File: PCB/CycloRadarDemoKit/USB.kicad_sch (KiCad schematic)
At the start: 41 parts, among them J301 USB_C_Receptacle_USB2.0, Q301 L8050QLT1G, Q302 L8050QLT1G, U301 CP2102N-Axx-xQFN28

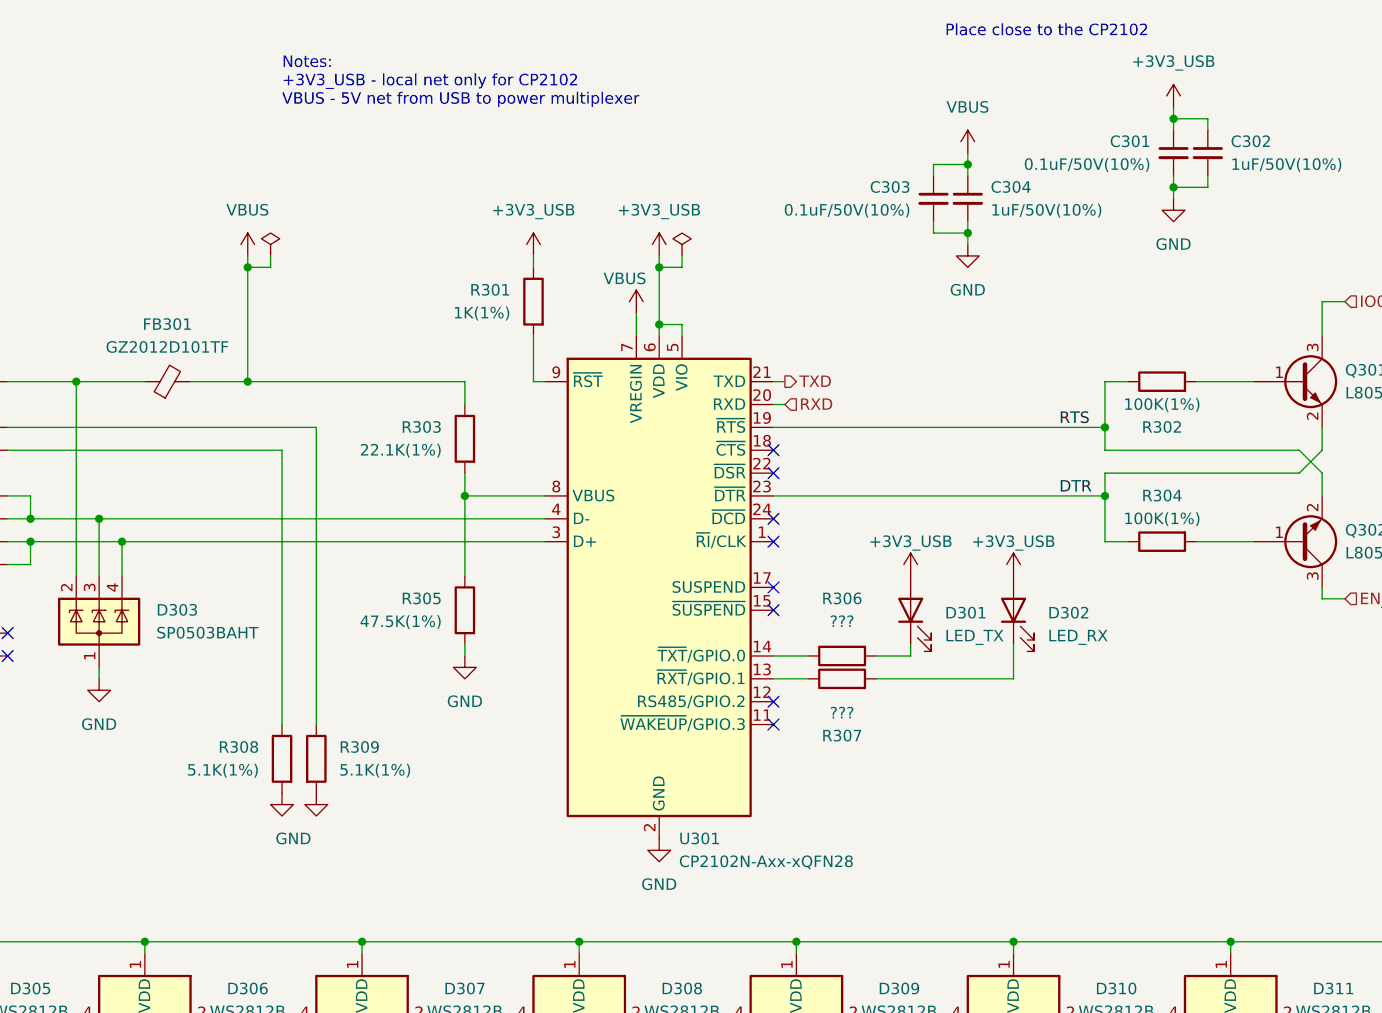
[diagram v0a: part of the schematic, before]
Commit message: added more LCSC parts
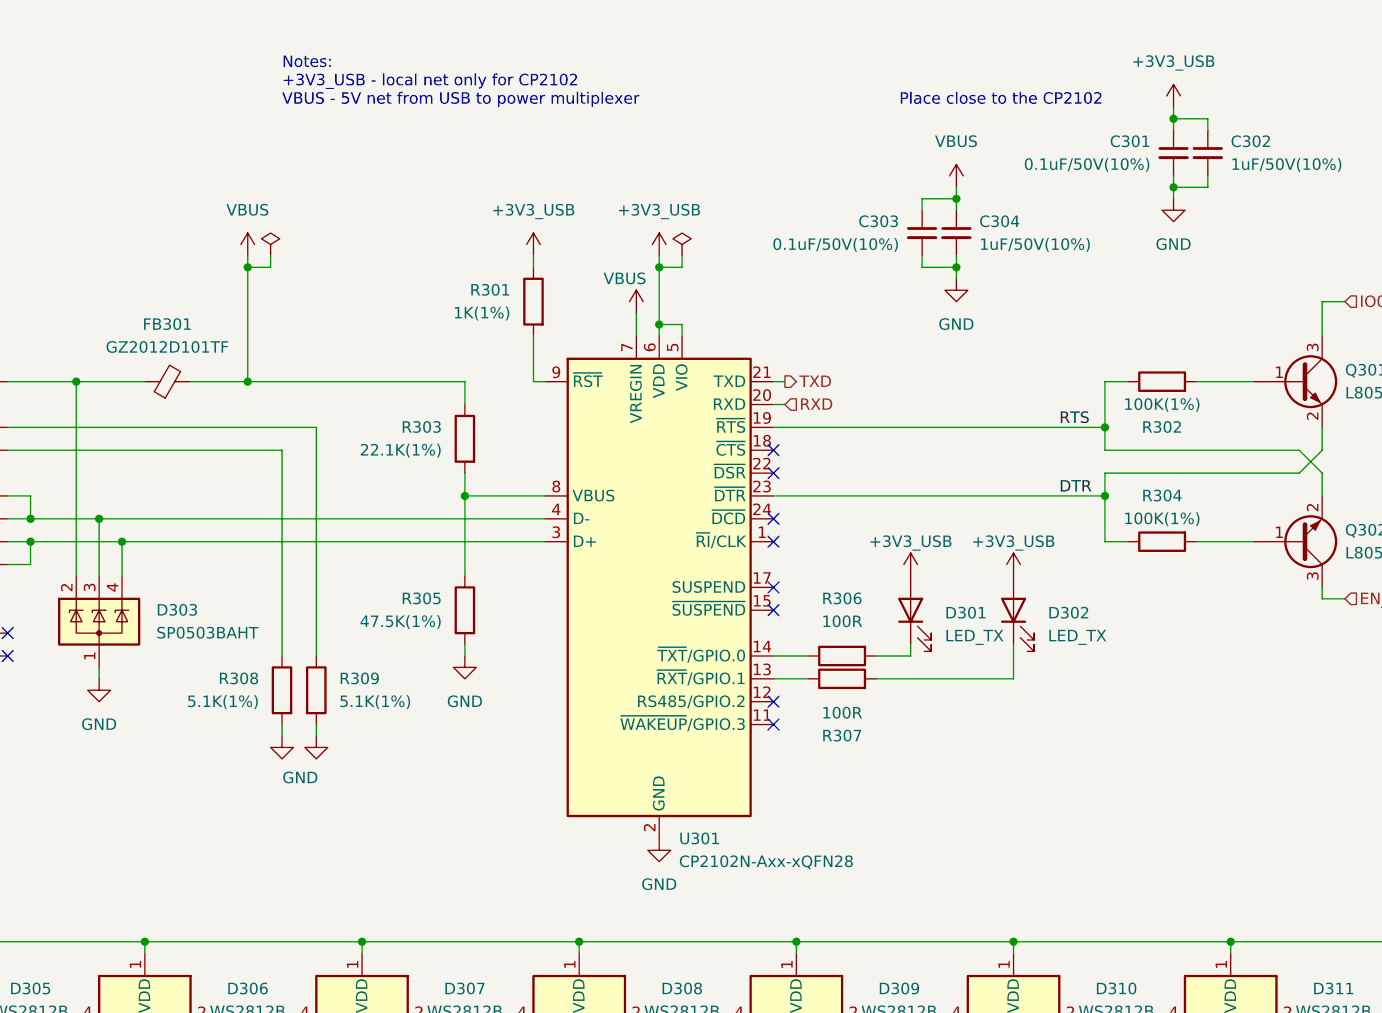
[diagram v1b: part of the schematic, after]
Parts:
- D301: footprint (none) -> LED_SMD:LED_0603_1608Metric; LCSC (none) -> C3028830
- D302: value LED_RX -> LED_TX; footprint (none) -> LED_SMD:LED_0603_1608Metric; LCSC (none) -> C3028830
- R301: footprint (none) -> Resistor_SMD:R_0603_1608Metric; LCSC (none) -> C21190
- R302, R304: footprint (none) -> Resistor_SMD:R_0603_1608Metric; LCSC (none) -> C25803
- R303: footprint (none) -> Resistor_SMD:R_0603_1608Metric; LCSC (none) -> C25961
- R305: footprint (none) -> Resistor_SMD:R_0603_1608Metric; LCSC (none) -> C23061
- R306, R307: value ??? -> 100R; footprint (none) -> Resistor_SMD:R_0603_1608Metric; LCSC (none) -> C22775
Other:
- moved on the sheet: C303, C304, R308, R309

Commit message: PCB ready for review
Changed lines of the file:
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@@
     (stroke (width 0) (type default))
   )
-  (wire (pts (xy 220.98 46.99) (xy 223.52 46.99))
+  (wire (pts (xy 220.98 49.53) (xy 223.52 49.53))
     (stroke (width 0) (type default))
   )
@@
     (stroke (width 0) (type default))
   )
-  (wire (pts (xy 220.98 50.8) (xy 220.98 46.99))
+  (wire (pts (xy 220.98 50.8) (xy 220.98 49.53))
     (stroke (width 0) (type default))
   )
@@
     (effects (font (size 1.27 1.27)) (justify left bottom))
   )
-  (hierarchical_label "IO0_AUTO" (shape input) (at 223.52 46.99 0) (fields_autoplaced)
+  (hierarchical_label "IO0_AUTO" (shape input) (at 223.52 49.53 0) (fields_autoplaced)
     (effects (font (size 1.27 1.27)) (justify left))
   )

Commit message: PCB after review
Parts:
- removed C301, C303: 0.1uF/50V(10%), Capacitor_SMD:C_0603_1608Metric, symbol Device:C_Small
- removed D304, D305, D306, D307, D308, D309, D310, D311, D312, D313, D314, D315, D316, D317, D318, D319, D320, D321, D322, D323: WS2812B, LED_SMD:LED_SK6812MINI_PLCC4_3.5x3.5mm_P1.75mm, symbol LED:WS2812B
- FB301: value GZ2012D101TF -> YI160808Z101-3R0T; footprint (none) -> Resistor_SMD:R_0603_1608Metric; LCSC (none) -> C3011210
- J301: footprint (none) -> Connector_USB:USB_C_Receptacle_GCT_USB4110; LCSC (none) -> C5260486
- renumbered C304 to C301
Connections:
- no-connect marks 12 -> 11
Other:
- note removed: "Place close to the CP2102"
- company: Alps Electric Czech, s.r.o. -> ALPS Electric Czech, s.r.o.
- title: Development module for Radar Safety Sensor -> Safety Ride Radar Sensor
- moved on the sheet: C301, C302, D301, D302, D303, FB301, J301, Q301, Q302, R301, R302, R303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

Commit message: updated readme
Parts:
- U301: value CP2102N-Axx-xQFN28 -> CP2102N-Axx-xQFN24
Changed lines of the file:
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@@
       (effects (font (size 1.27 1.27)) (justify left))
     )
-    (property "Value" "CP2102N-Axx-xQFN28" (at 159.6741 139.7 0)
+    (property "Value" "CP2102N-Axx-xQFN24" (at 159.6741 139.7 0)
       (effects (font (size 1.27 1.27)) (justify left))
     )

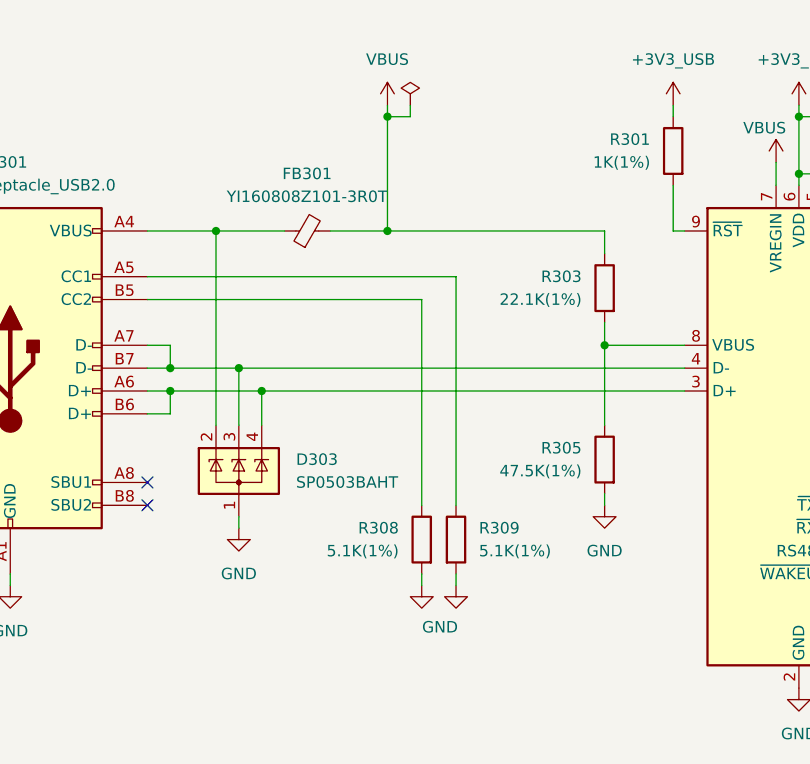
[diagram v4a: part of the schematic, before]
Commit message: schematic cosmetics, power management diagram upgrated
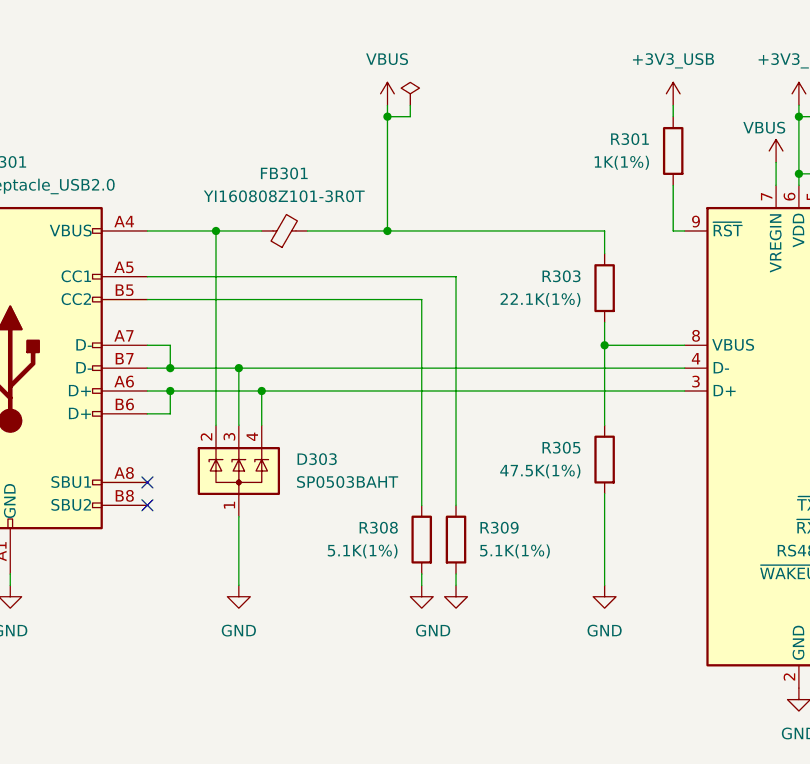
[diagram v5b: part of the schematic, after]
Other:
- moved on the sheet: FB301
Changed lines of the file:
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@@
     (stroke (width 0) (type default))
   )
-  (wire (pts (xy 95.25 118.11) (xy 95.25 119.38))
+  (wire (pts (xy 95.25 118.11) (xy 95.25 125.73))
     (stroke (width 0) (type default))
   )
@@
     (stroke (width 0) (type default))
   )
-  (wire (pts (xy 105.41 86.36) (xy 111.76 86.36))
+  (wire (pts (xy 102.87 86.36) (xy 111.76 86.36))
     (stroke (width 0) (type default))
   )
@@
     (stroke (width 0) (type default))
   )
-  (wire (pts (xy 92.71 86.36) (xy 100.33 86.36))
+  (wire (pts (xy 92.71 86.36) (xy 97.79 86.36))
     (stroke (width 0) (type default))
   )
@@
     (stroke (width 0) (type default))
   )
-  (wire (pts (xy 135.89 115.57) (xy 135.89 116.84))
+  (wire (pts (xy 135.89 115.57) (xy 135.89 125.73))
     (stroke (width 0) (type default))
   )
@@
     (effects (font (size 1.27 1.27)) (justify left))
   )
-  (symbol (lib_id "power:GND") (at 135.89 116.84 0) (unit 1)
-    (in_bom yes) (on_board yes) (dnp no) (fields_autoplaced)
-    (property "Reference" "#PWR0311" (at 135.89 123.19 0)
-      (effects (font (size 1.27 1.27)) hide)
-    )
-    (property "Value" "GND" (at 135.89 121.92 0)
-      (effects (font (size 1.27 1.27)))
-    )
-    (property "Footprint" "" (at 135.89 116.84 0)
-      (effects (font (size 1.27 1.27)) hide)
-    )
-    (property "Datasheet" "" (at 135.89 116.84 0)
+  (symbol (lib_id "power:GND") (at 135.89 125.73 0) (unit 1)
+    (in_bom yes) (on_board yes) (dnp no) (fields_autoplaced)
+    (property "Reference" "#PWR0311" (at 135.89 132.08 0)
+      (effects (font (size 1.27 1.27)) hide)
+    )
+    (property "Value" "GND" (at 135.89 130.81 0)
+      (effects (font (size 1.27 1.27)))
+    )
+    (property "Footprint" "" (at 135.89 125.73 0)
+      (effects (font (size 1.27 1.27)) hide)
+    )
+    (property "Datasheet" "" (at 135.89 125.73 0)
       (effects (font (size 1.27 1.27)) hide)
     )
@@
       (effects (font (size 1.27 1.27)) hide)
     )
-    (property "Value" "GND" (at 117.6006 130.3838 0)
+    (property "Value" "GND" (at 116.84 130.81 0)
       (effects (font (size 1.27 1.27)))
     )
@@
     )
   )
-  (symbol (lib_id "power:GND") (at 95.25 119.38 0) (unit 1)
-    (in_bom yes) (on_board yes) (dnp no) (fields_autoplaced)
-    (property "Reference" "#PWR0312" (at 95.25 125.73 0)
-      (effects (font (size 1.27 1.27)) hide)
-    )
-    (property "Value" "GND" (at 95.25 124.46 0)
-      (effects (font (size 1.27 1.27)))
-    )
-    (property "Footprint" "" (at 95.25 119.38 0)
-      (effects (font (size 1.27 1.27)) hide)
-    )
-    (property "Datasheet" "" (at 95.25 119.38 0)
+  (symbol (lib_id "power:GND") (at 95.25 125.73 0) (unit 1)
+    (in_bom yes) (on_board yes) (dnp no) (fields_autoplaced)
+    (property "Reference" "#PWR0312" (at 95.25 132.08 0)
+      (effects (font (size 1.27 1.27)) hide)
+    )
+    (property "Value" "GND" (at 95.25 130.81 0)
+      (effects (font (size 1.27 1.27)))
+    )
+    (property "Footprint" "" (at 95.25 125.73 0)
+      (effects (font (size 1.27 1.27)) hide)
+    )
+    (property "Datasheet" "" (at 95.25 125.73 0)
       (effects (font (size 1.27 1.27)) hide)
     )
@@
     )
   )
-  (symbol (lib_id "Device:FerriteBead_Small") (at 102.87 86.36 90) (unit 1)
-    (in_bom yes) (on_board yes) (dnp no) (fields_autoplaced)
-    (property "Reference" "FB301" (at 102.8319 80.01 90)
-      (effects (font (size 1.27 1.27)))
-    )
-    (property "Value" "YI160808Z101-3R0T" (at 102.8319 82.55 90)
-      (effects (font (size 1.27 1.27)))
-    )
-    (property "Footprint" "Resistor_SMD:R_0603_1608Metric" (at 102.87 88.138 90)
-      (effects (font (size 1.27 1.27)) hide)
-    )
-    (property "Datasheet" "~" (at 102.87 86.36 0)
-      (effects (font (size 1.27 1.27)) hide)
-    )
-    (property "LCSC" "C3011210" (at 102.87 86.36 0)
-      (effects (font (size 1.27 1.27)) hide)
-    )
+  (symbol (lib_id "Device:FerriteBead_Small") (at 100.33 86.36 90) (unit 1)
+    (in_bom yes) (on_board yes) (dnp no) (fields_autoplaced)
+    (property "Reference" "FB301" (at 100.2919 80.01 90)
+      (effects (font (size 1.27 1.27)))
+    )
+    (property "Value" "YI160808Z101-3R0T" (at 100.2919 82.55 90)
+      (effects (font (size 1.27 1.27)))
+    )
+    (property "Footprint" "Resistor_SMD:R_0603_1608Metric" (at 100.33 88.138 90)
+      (effects (font (size 1.27 1.27)) hide)
+    )
+    (property "Datasheet" "~" (at 100.33 86.36 0)
+      (effects (font (size 1.27 1.27)) hide)
+    )
+    (property "LCSC" "C3011210" (at 100.33 86.36 0)
+      (effects (font (size 1.27 1.27)) hide)
+    )

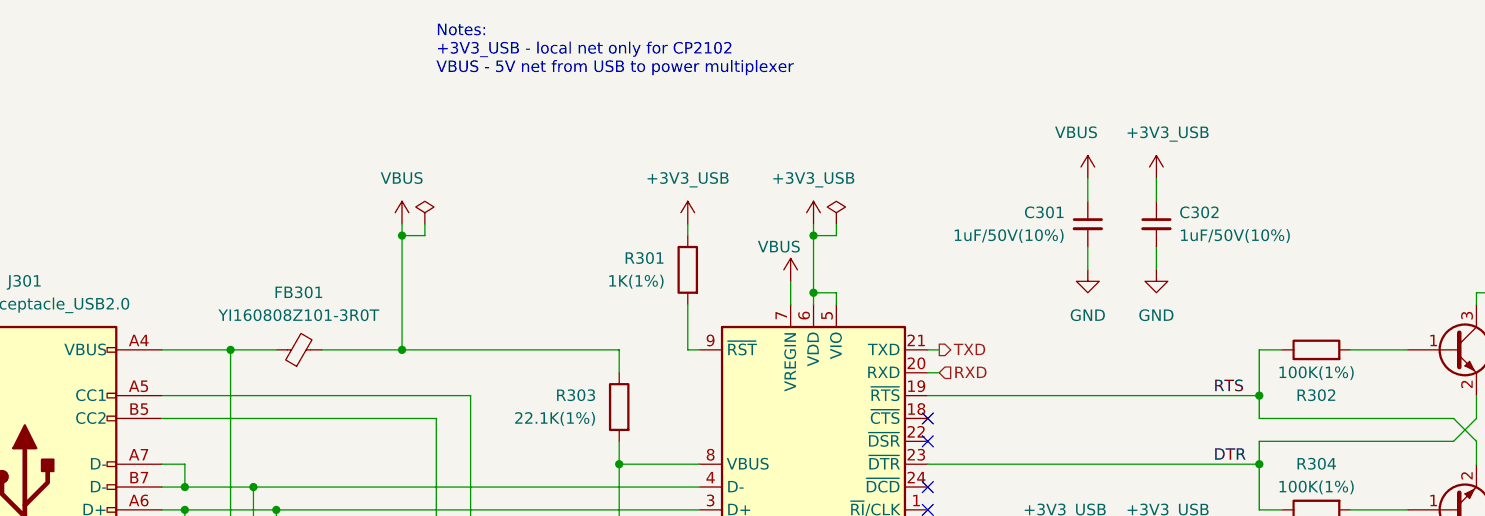
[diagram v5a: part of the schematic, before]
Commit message: Schematic edited, split sheets
improved PM diagram
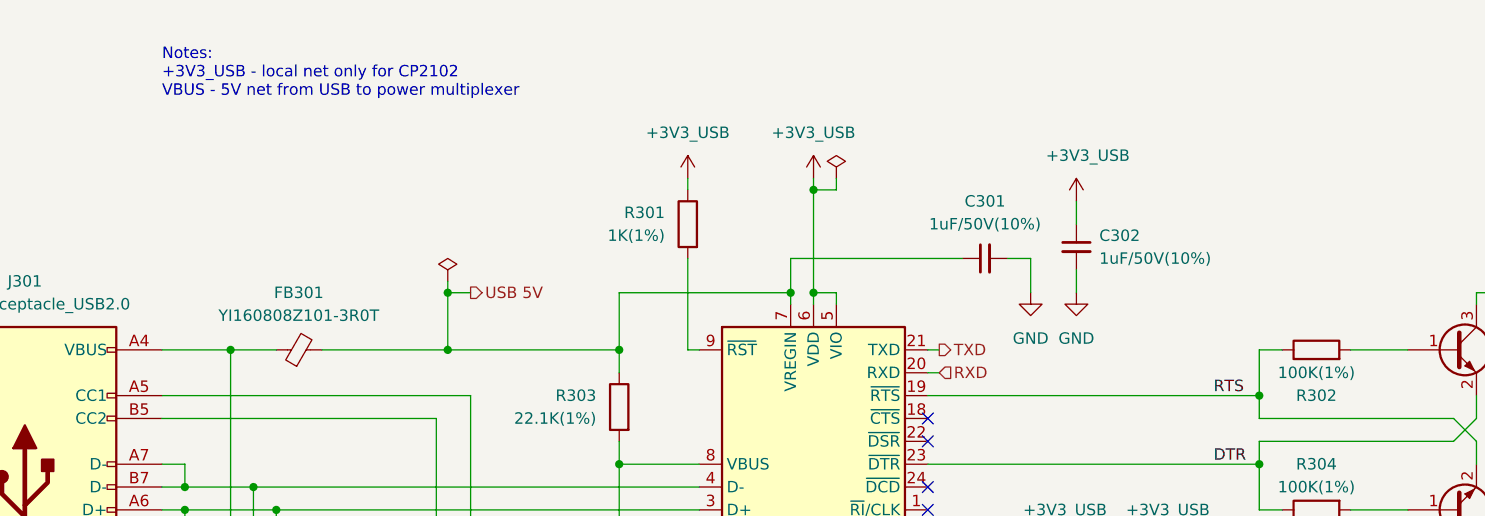
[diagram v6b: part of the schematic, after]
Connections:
- net VBUS renamed USB 5V
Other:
- moved on the sheet: C301, C302, R301

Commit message: PCB, 3Dmodel
mockup PCB version done, schcematic exported to latex, 3D model generated and exported to latex
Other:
- title: Safety Ride Radar Sensor -> Radar Safety Sensor
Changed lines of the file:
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@@
   (paper "A4")
   (title_block
-    (title "Safety Ride Radar Sensor")
-    (date "2023-12-19")
-    (rev "Rev.: WIP")
+    (title "Radar Safety Sensor")
+    (date "2023-12-20")
+    (rev "Rev.: 1")
     (company "ALPS Electric Czech, s.r.o.")
     (comment 1 "Designed by Martin Tavoda")
